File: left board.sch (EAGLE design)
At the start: 50 parts, among them IC1 LM555D, IC2 LM555D, Q1 10, Q2 10

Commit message: all gerbers generated
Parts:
- added H1, H2, H3, H4: STAND-OFF, SparkFun-Electromechanical:STAND-OFF
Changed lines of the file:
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@@
 <part name="Q2" library="transistor-power" library_urn="urn:adsk.eagle:library:400" deviceset="PMOSFET_N" device="TO220BV" package3d_urn="urn:adsk.eagle:package:29484/1" value="10"/>
 <part name="Q1" library="transistor-power" library_urn="urn:adsk.eagle:library:400" deviceset="PMOSFET_N" device="TO220BV" package3d_urn="urn:adsk.eagle:package:29484/1" value="10"/>
+<part name="H1" library="SparkFun-Electromechanical" deviceset="STAND-OFF" device=""/>
+<part name="H2" library="SparkFun-Electromechanical" deviceset="STAND-OFF" device=""/>
+<part name="H3" library="SparkFun-Electromechanical" deviceset="STAND-OFF" device=""/>
+<part name="H4" library="SparkFun-Electromechanical" deviceset="STAND-OFF" device=""/>
 </parts>
 <sheets>
@@
 <instance part="Q2" gate="G$1" x="-114.3" y="-5.08" rot="R180"/>
 <instance part="Q1" gate="G$1" x="50.8" y="-5.08" rot="R180"/>
+<instance part="H1" gate="G$1" x="66.04" y="33.02"/>
+<instance part="H2" gate="G$1" x="73.66" y="33.02"/>
+<instance part="H3" gate="G$1" x="81.28" y="33.02"/>
+<instance part="H4" gate="G$1" x="88.9" y="33.02"/>
 </instances>
 <busses>

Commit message: via gerbers generated
via boards completed and gerbers generated
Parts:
- removed Q1, Q2: 10, transistor-power:PMOSFET_NTO220BV
- added Q3, Q4: BSS101, transistor-fet:BSS101
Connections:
- net B_BLINK: now also Q3.S; no longer Q2.S
- net B_OUT: now also Q3.G; no longer Q2.G
- net D_BLINK: now also Q4.S; no longer Q1.S
- net D_OUT: now also Q4.G; no longer Q1.G
- net N$1: now also Q3.D; no longer Q2.D
- net N$11: now also Q4.D; no longer Q1.D
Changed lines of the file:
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@@
 <part name="U$3" library="SparkFun-Resistors" deviceset="10K_LINEAR_POT_SMD" device=""/>
 <part name="U$4" library="SparkFun-Resistors" deviceset="10K_LINEAR_POT_SMD" device=""/>
-<part name="Q2" library="transistor-power" library_urn="urn:adsk.eagle:library:400" deviceset="PMOSFET_N" device="TO220BV" package3d_urn="urn:adsk.eagle:package:29484/1" value="10"/>
-<part name="Q1" library="transistor-power" library_urn="urn:adsk.eagle:library:400" deviceset="PMOSFET_N" device="TO220BV" package3d_urn="urn:adsk.eagle:package:29484/1" value="10"/>
 <part name="H1" library="SparkFun-Electromechanical" deviceset="STAND-OFF" device=""/>
 <part name="H2" library="SparkFun-Electromechanical" deviceset="STAND-OFF" device=""/>
 <part name="H3" library="SparkFun-Electromechanical" deviceset="STAND-OFF" device=""/>
 <part name="H4" library="SparkFun-Electromechanical" deviceset="STAND-OFF" device=""/>
+<part name="Q3" library="transistor-fet" library_urn="urn:adsk.eagle:library:396" deviceset="BSS101" device="" package3d_urn="urn:adsk.eagle:package:28523/1"/>
+<part name="Q4" library="transistor-fet" library_urn="urn:adsk.eagle:library:396" deviceset="BSS101" device="" package3d_urn="urn:adsk.eagle:package:28523/1"/>
 </parts>
 <sheets>
@@
 <instance part="U$3" gate="G$1" x="-38.1" y="-17.78" rot="R180"/>
 <instance part="U$4" gate="G$1" x="127" y="-17.78" rot="R180"/>
-<instance part="Q2" gate="G$1" x="-114.3" y="-5.08" rot="R180"/>
-<instance part="Q1" gate="G$1" x="50.8" y="-5.08" rot="R180"/>
 <instance part="H1" gate="G$1" x="66.04" y="33.02"/>
 <instance part="H2" gate="G$1" x="73.66" y="33.02"/>
 <instance part="H3" gate="G$1" x="81.28" y="33.02"/>
 <instance part="H4" gate="G$1" x="88.9" y="33.02"/>
+<instance part="Q3" gate="G$1" x="-111.76" y="-2.54" rot="R180"/>
+<instance part="Q4" gate="G$1" x="48.26" y="-5.08" rot="R180"/>
 </instances>
 <busses>
@@
 </segment>
 <segment>
-<wire x1="-109.22" y1="-2.54" x2="-109.22" y2="-40.64" width="0.1524" layer="91"/>
+<wire x1="-101.6" y1="0" x2="-109.22" y2="-40.64" width="0.1524" layer="91"/>
 <label x="-109.22" y="-40.64" size="1.778" layer="95" rot="R90"/>
-<pinref part="Q2" gate="G$1" pin="G"/>
-<wire x1="-111.76" y1="-2.54" x2="-109.22" y2="-2.54" width="0.1524" layer="91"/>
+<pinref part="Q3" gate="G$1" pin="G"/>
+<wire x1="-106.68" y1="0" x2="-101.6" y2="0" width="0.1524" layer="91"/>
 </segment>
 </net>
@@
 <wire x1="55.88" y1="-2.54" x2="55.88" y2="-33.02" width="0.1524" layer="91"/>
 <label x="55.88" y="-33.02" size="1.778" layer="95" rot="R90"/>
-<pinref part="Q1" gate="G$1" pin="G"/>
 <wire x1="53.34" y1="-2.54" x2="55.88" y2="-2.54" width="0.1524" layer="91"/>
+<pinref part="Q4" gate="G$1" pin="G"/>
 </segment>
 </net>
@@
 <wire x1="127" y1="10.16" x2="127" y2="12.7" width="0.1524" layer="91"/>
 <junction x="127" y="12.7"/>
-<wire x1="48.26" y1="0" x2="48.26" y2="12.7" width="0.1524" layer="91"/>
+<wire x1="48.26" y1="-2.54" x2="48.26" y2="12.7" width="0.1524" layer="91"/>
 <junction x="48.26" y="12.7"/>
 <pinref part="R8" gate="G$1" pin="2"/>
-<pinref part="Q1" gate="G$1" pin="S"/>
+<pinref part="Q4" gate="G$1" pin="S"/>
+<wire x1="43.18" y1="-2.54" x2="48.26" y2="-2.54" width="0.1524" layer="91"/>
 </segment>
 </net>
@@
 <junction x="-116.84" y="12.7"/>
 <pinref part="R9" gate="G$1" pin="2"/>
-<pinref part="Q2" gate="G$1" pin="S"/>
+<pinref part="Q3" gate="G$1" pin="S"/>
 </segment>
 </net>
@@
 <wire x1="48.26" y1="-17.78" x2="63.5" y2="-17.78" width="0.1524" layer="91"/>
 <pinref part="R14" gate="G$1" pin="1"/>
-<pinref part="Q1" gate="G$1" pin="D"/>
-<wire x1="48.26" y1="-10.16" x2="48.26" y2="-17.78" width="0.1524" layer="91"/>
+<wire x1="48.26" y1="-7.62" x2="48.26" y2="-17.78" width="0.1524" layer="91"/>
+<pinref part="Q4" gate="G$1" pin="D"/>
+<wire x1="43.18" y1="-7.62" x2="48.26" y2="-7.62" width="0.1524" layer="91"/>
 </segment>
 </net>
@@
 <wire x1="-116.84" y1="-17.78" x2="-101.6" y2="-17.78" width="0.1524" layer="91"/>
 <pinref part="R11" gate="G$1" pin="2"/>
-<pinref part="Q2" gate="G$1" pin="D"/>
-<wire x1="-116.84" y1="-10.16" x2="-116.84" y2="-17.78" width="0.1524" layer="91"/>
-</segment>
-</net>
+<wire x1="-116.84" y1="-5.08" x2="-116.84" y2="-17.78" width="0.1524" layer="91"/>
+<pinref part="Q3" gate="G$1" pin="D"/>
+</segment>
+</net>

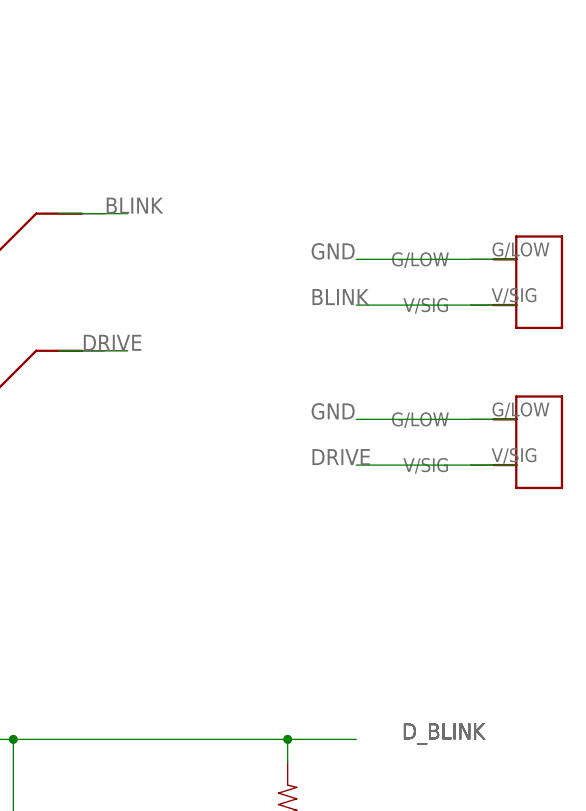
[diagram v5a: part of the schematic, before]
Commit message: added reverse polairity protection
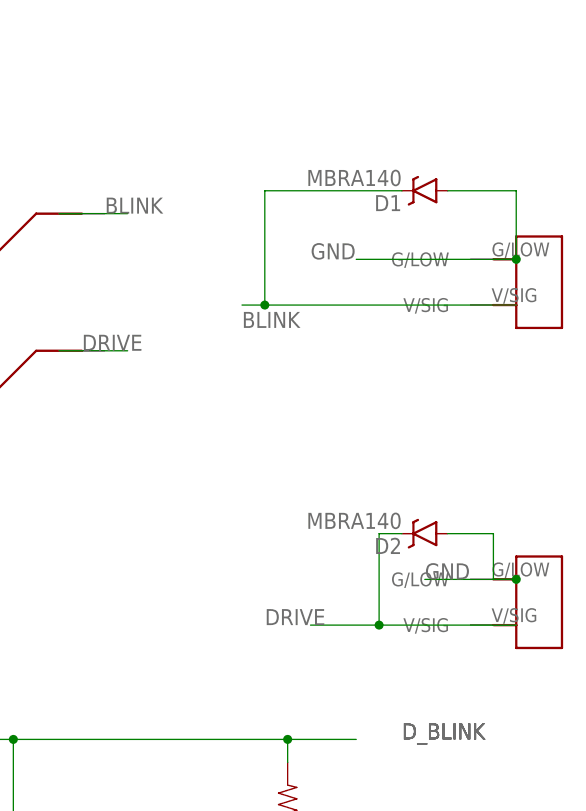
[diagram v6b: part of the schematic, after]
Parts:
- removed L_DRIVE: 2_PIN_TECONNECTOR, TE 2-pin connector:2_PIN_TECONNECTOR
- added D1, D2: MBRA140, SparkFun-DiscreteSemi:MBRA140
- added U$5: 2_PIN_TECONNECTOR, TE 2-pin connector:2_PIN_TECONNECTOR
- renumbered L_BLINK to U$7
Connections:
- net BLINK: now also D1.C
- net DRIVE: now also D2.C, U$5.V/SIG; no longer L_DRIVE.V/SIG
- net GND: now also D1.A, D2.A, U$5.G/LOW; no longer L_DRIVE.G/LOW
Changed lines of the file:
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@@
 <?xml version="1.0" encoding="utf-8"?>
 <!DOCTYPE eagle SYSTEM "eagle.dtd">
-<eagle version="8.3.1">
+<eagle version="8.6.1">
 <drawing>
 <settings>
@@
 <layer number="230" name="230bmp" color="7" fill="1" visible="yes" active="yes"/>
 <layer number="231" name="231bmp" color="7" fill="1" visible="yes" active="yes"/>
+<layer number="232" name="Eagle3D_PG2" color="7" fill="1" visible="no" active="no"/>
+<layer number="233" name="Eagle3D_PG3" color="7" fill="1" visible="no" active="no"/>
 <layer number="248" name="Housing" color="7" fill="1" visible="yes" active="yes"/>
 <layer number="249" name="Edge" color="7" fill="1" visible="yes" active="yes"/>
@@
 </classes>
 <parts>
-<part name="L_DRIVE" library="TE 2-pin connector" deviceset="2_PIN_TECONNECTOR" device=""/>
-<part name="L_BLINK" library="TE 2-pin connector" deviceset="2_PIN_TECONNECTOR" device=""/>
 <part name="IC1" library="linear" library_urn="urn:adsk.eagle:library:262" deviceset="*555" device="D" package3d_urn="urn:adsk.eagle:package:16404/2" technology="LM"/>
 <part name="GND1" library="E-P-008-R1.2" deviceset="GND" device=""/>
@@
 <part name="Q3" library="transistor-fet" library_urn="urn:adsk.eagle:library:396" deviceset="BSS101" device="" package3d_urn="urn:adsk.eagle:package:28523/1"/>
 <part name="Q4" library="transistor-fet" library_urn="urn:adsk.eagle:library:396" deviceset="BSS101" device="" package3d_urn="urn:adsk.eagle:package:28523/1"/>
+<part name="U$5" library="TE 2-pin connector" deviceset="2_PIN_TECONNECTOR" device=""/>
+<part name="U$7" library="TE 2-pin connector" deviceset="2_PIN_TECONNECTOR" device=""/>
+<part name="D1" library="SparkFun-DiscreteSemi" deviceset="MBRA140" device=""/>
+<part name="D2" library="SparkFun-DiscreteSemi" deviceset="MBRA140" device=""/>
 </parts>
 <sheets>
@@
 </plain>
 <instances>
-<instance part="L_DRIVE" gate="G$1" x="157.48" y="45.72"/>
-<instance part="L_BLINK" gate="G$1" x="157.48" y="63.5"/>
 <instance part="IC1" gate="A" x="-81.28" y="-15.24"/>
 <instance part="GND1" gate="1" x="-48.26" y="-40.64"/>
@@
 <instance part="Q3" gate="G$1" x="-111.76" y="-2.54" rot="R180"/>
 <instance part="Q4" gate="G$1" x="48.26" y="-5.08" rot="R180"/>
+<instance part="U$5" gate="G$1" x="157.48" y="27.94"/>
+<instance part="U$7" gate="G$1" x="157.48" y="63.5"/>
+<instance part="D1" gate="G$1" x="142.24" y="73.66" rot="R180"/>
+<instance part="D2" gate="G$1" x="142.24" y="35.56" rot="R180"/>
 </instances>
 <busses>
@@
 </segment>
 <segment>
-<pinref part="L_BLINK" gate="G$1" pin="G/LOW"/>
 <wire x1="152.4" y1="66.04" x2="134.62" y2="66.04" width="0.1524" layer="91"/>
 <label x="129.54" y="66.04" size="1.778" layer="95"/>
-</segment>
-<segment>
-<pinref part="L_DRIVE" gate="G$1" pin="G/LOW"/>
-<wire x1="152.4" y1="48.26" x2="134.62" y2="48.26" width="0.1524" layer="91"/>
-<label x="129.54" y="48.26" size="1.778" layer="95"/>
+<pinref part="U$7" gate="G$1" pin="G/LOW"/>
+<pinref part="D1" gate="G$1" pin="A"/>
+<wire x1="144.78" y1="73.66" x2="152.4" y2="73.66" width="0.1524" layer="91"/>
+<wire x1="152.4" y1="73.66" x2="152.4" y2="66.04" width="0.1524" layer="91"/>
+<junction x="152.4" y="66.04"/>
+</segment>
+<segment>
+<wire x1="152.4" y1="30.48" x2="142.24" y2="30.48" width="0.1524" layer="91"/>
+<label x="142.24" y="30.48" size="1.778" layer="95"/>
+<pinref part="U$5" gate="G$1" pin="G/LOW"/>
+<wire x1="152.4" y1="30.48" x2="149.86" y2="30.48" width="0.1524" layer="91"/>
+<wire x1="149.86" y1="30.48" x2="149.86" y2="35.56" width="0.1524" layer="91"/>
+<junction x="152.4" y="30.48"/>
+<pinref part="D2" gate="G$1" pin="A"/>
+<wire x1="149.86" y1="35.56" x2="144.78" y2="35.56" width="0.1524" layer="91"/>
 </segment>
 <segment>
@@
 <net name="BLINK" class="0">
 <segment>
-<pinref part="L_BLINK" gate="G$1" pin="V/SIG"/>
-<wire x1="152.4" y1="60.96" x2="134.62" y2="60.96" width="0.1524" layer="91"/>
-<label x="129.54" y="60.96" size="1.778" layer="95"/>
+<wire x1="152.4" y1="60.96" x2="124.46" y2="60.96" width="0.1524" layer="91"/>
+<label x="121.92" y="58.42" size="1.778" layer="95"/>
+<pinref part="U$7" gate="G$1" pin="V/SIG"/>
+<pinref part="D1" gate="G$1" pin="C"/>
+<wire x1="124.46" y1="60.96" x2="121.92" y2="60.96" width="0.1524" layer="91"/>
+<wire x1="139.7" y1="73.66" x2="124.46" y2="73.66" width="0.1524" layer="91"/>
+<wire x1="124.46" y1="73.66" x2="124.46" y2="60.96" width="0.1524" layer="91"/>
+<junction x="124.46" y="60.96"/>
 </segment>
 <segment>
@@
 <net name="DRIVE" class="0">
 <segment>
-<pinref part="L_DRIVE" gate="G$1" pin="V/SIG"/>
-<wire x1="152.4" y1="43.18" x2="134.62" y2="43.18" width="0.1524" layer="91"/>
-<label x="129.54" y="43.18" size="1.778" layer="95"/>
-</segment>
-<segment>
+<wire x1="152.4" y1="25.4" x2="137.16" y2="25.4" width="0.1524" layer="91"/>
+<label x="124.46" y="25.4" size="1.778" layer="95"/>
+<pinref part="U$5" gate="G$1" pin="V/SIG"/>
+<pinref part="D2" gate="G$1" pin="C"/>
+<wire x1="139.7" y1="35.56" x2="137.16" y2="35.56" width="0.1524" layer="91"/>
+<wire x1="137.16" y1="35.56" x2="137.16" y2="25.4" width="0.1524" layer="91"/>
+<junction x="137.16" y="25.4"/>
+<wire x1="137.16" y1="25.4" x2="129.54" y2="25.4" width="0.1524" layer="91"/>
+</segment>
+<segment>
